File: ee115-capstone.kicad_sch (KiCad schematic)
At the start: 0 parts

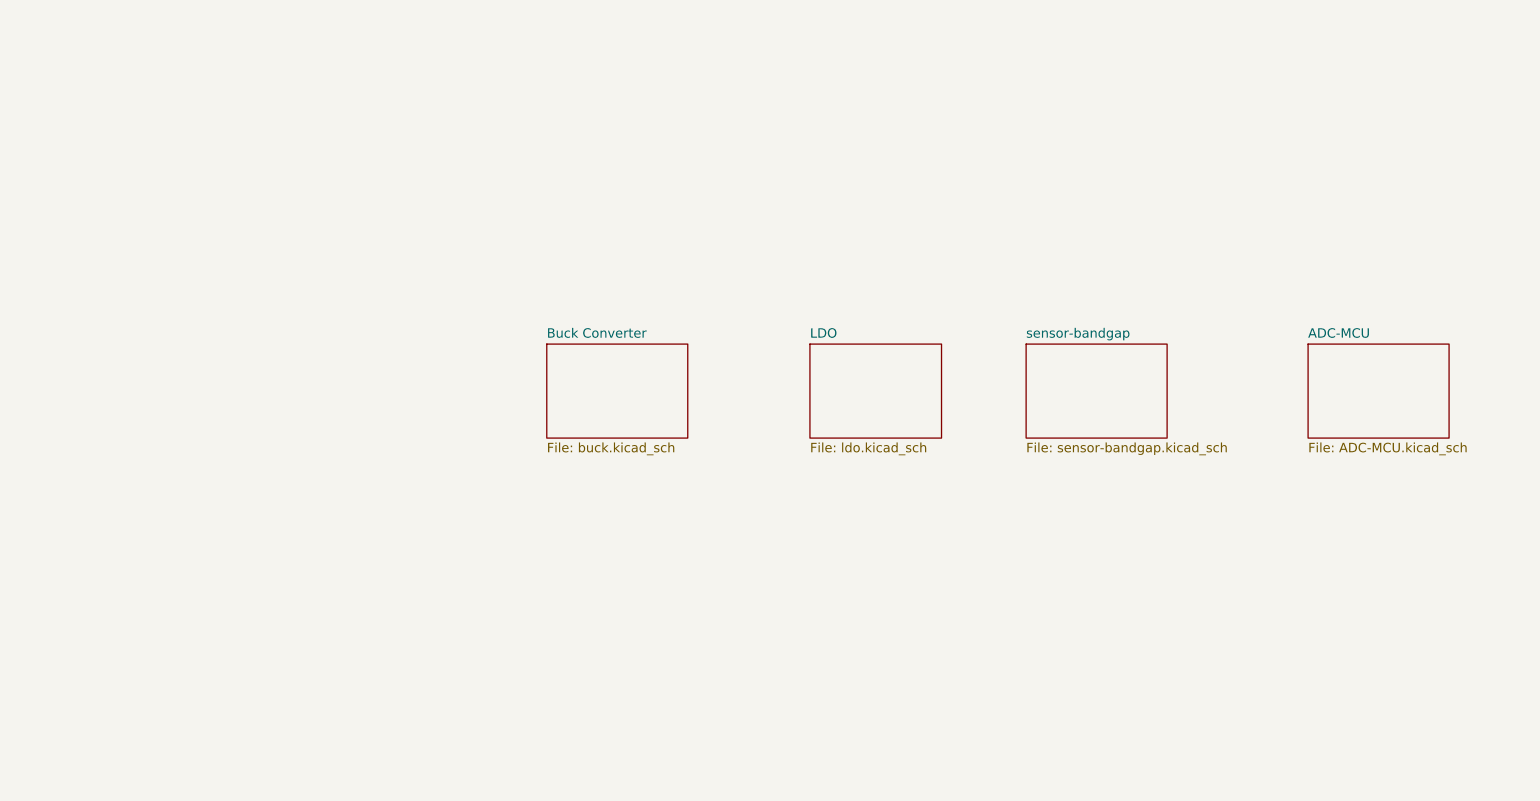
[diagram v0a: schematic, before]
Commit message: ADC-MCU and power latch
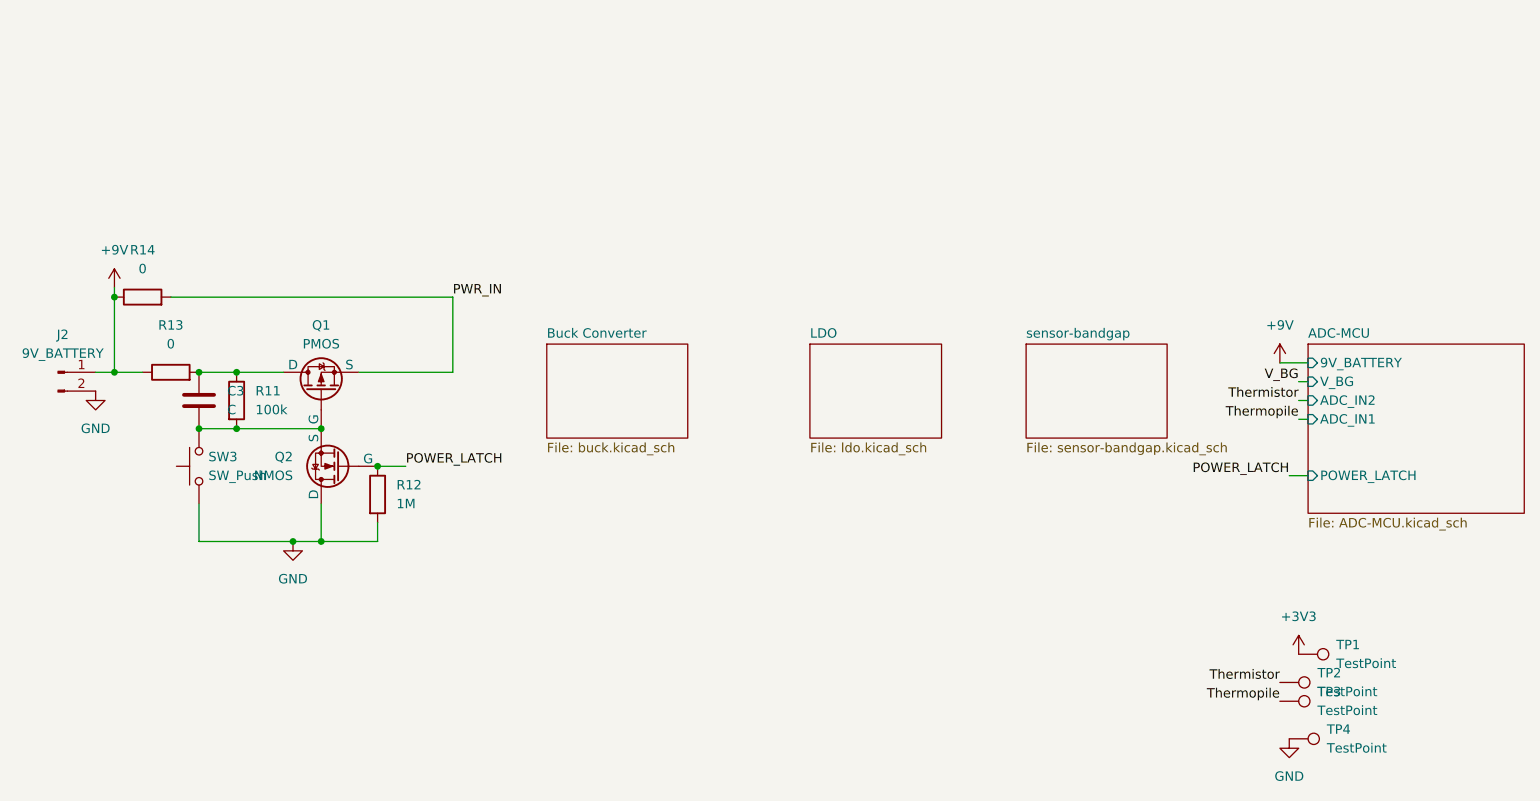
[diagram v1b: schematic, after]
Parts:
- added C3: C, Capacitor_SMD:C_0805_2012Metric, symbol Device:C
- added J2: 9V_BATTERY, Connector_JST:JST_PH_B2B-PH-K_1x02_P2.00mm_Vertical, symbol Connector:Conn_01x02_Pin
- added Q1: PMOS, symbol Simulation_SPICE:PMOS
- added Q2: NMOS, symbol Simulation_SPICE:NMOS
- added R11: 100k, Resistor_SMD:R_0805_2012Metric, symbol Device:R
- added R12: 1M, Resistor_SMD:R_0805_2012Metric, symbol Device:R
- added R13, R14: 0, Resistor_SMD:R_0805_2012Metric, symbol Device:R
- added SW3: SW_Push, Button_Switch_THT:SW_PUSH_6mm, symbol Switch:SW_Push
- added TP1, TP2, TP3, TP4: TestPoint, Connector_Pin:Pin_D1.0mm_L10.0mm, symbol Connector:TestPoint
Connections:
- new net: C3.1, Q1.1 (D), R11.1, R13.2
- new net: C3.2, Q1.2 (G), Q2.3 (S), R11.2, SW3.2
- new net +3V3: TP1.1
- new net +9V: J2.1 (Pin_1), R13.1, R14.1
- new net GND: J2.2 (Pin_2), Q2.1 (D), R12.2, SW3.1, TP4.1
- new net POWER_LATCH: Q2.2 (G), R12.1
- new net PWR_IN: Q1.3 (S), R14.2
- new net Thermistor: TP2.1
- new net Thermopile: TP3.1
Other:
- sheet ADC-MCU ports: added 9V_BATTERY, ADC_IN1, ADC_IN2, POWER_LATCH, V_BG; removed none

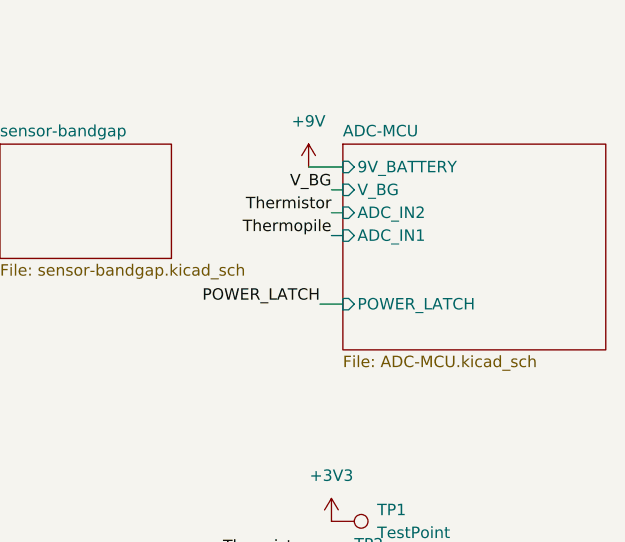
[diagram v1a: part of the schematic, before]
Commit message: added range sel
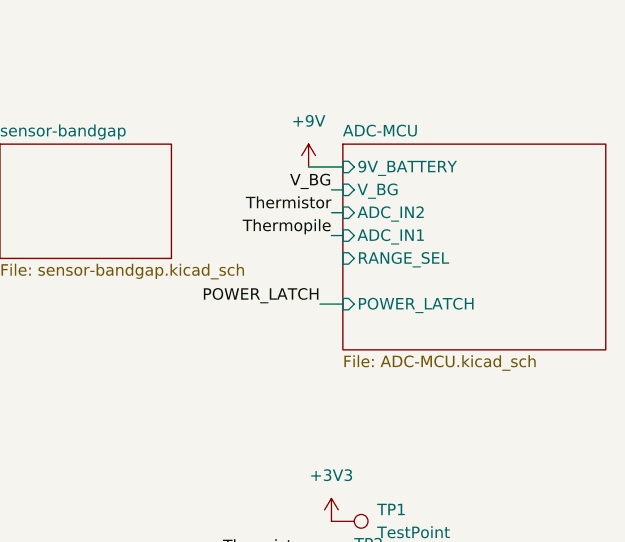
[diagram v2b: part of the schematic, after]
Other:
- sheet ADC-MCU ports: added RANGE_SEL; removed none
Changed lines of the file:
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@@
+			)
+		)
+		(pin "RANGE_SEL" input
+			(at 193.04 72.39 180)
+			(effects
+				(font
+					(size 1.27 1.27)
+				)
+				(justify left)
 			)
 		)

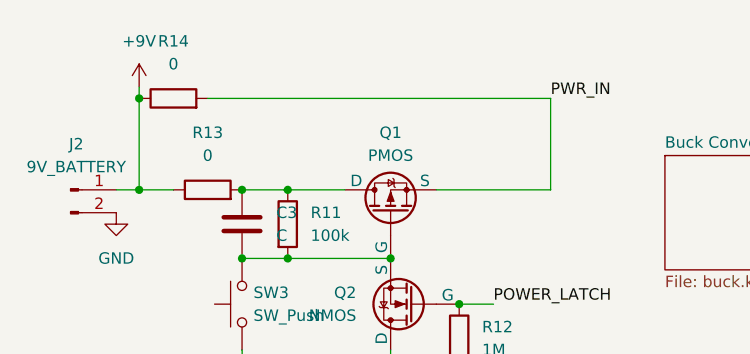
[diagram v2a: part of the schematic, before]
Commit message: added spst as backup to power latch
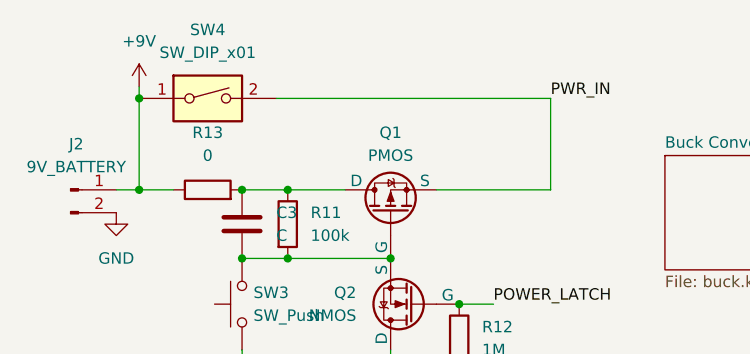
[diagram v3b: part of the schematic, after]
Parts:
- removed R14: 0, Resistor_SMD:R_0805_2012Metric, symbol Device:R
- added SW4: SW_DIP_x01, symbol Switch:SW_DIP_x01
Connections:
- net +9V: now also SW4.1
- net PWR_IN: now also SW4.2
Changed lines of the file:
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@@
+	)
+	(junction
+		(at 48.26 71.12)
+		(diameter 0)
+		(color 0 0 0 0)
+	)
+	(junction
+		(at 43.18 71.12)
+		(diameter 0)
+		(color 0 0 0 0)
+	)
+	(junction
+		(at 31.75 63.5)
+		(diameter 0)
+		(color 0 0 0 0)
 	)
 	(junction
@@
 		(color 0 0 0 0)
 	)
-	(junction
-		(at 48.26 71.12)
-		(diameter 0)
-		(color 0 0 0 0)
-	)
-	(junction
-		(at 43.18 71.12)
-		(diameter 0)
-		(color 0 0 0 0)
-	)
-	(junction
-		(at 31.75 63.5)
-		(diameter 0)
-		(color 0 0 0 0)
-	)
 	(wire
 		(pts
@@
 	(wire
 		(pts
+			(xy 46.99 53.34) (xy 77.47 53.34)
+		)
+		(stroke
+			(width 0)
+			(type default)
+		)
+	)
+	(wire
+		(pts
 			(xy 31.75 52.07) (xy 31.75 53.34)
 		)
@@
 	(wire
 		(pts
+			(xy 31.75 53.34) (xy 31.75 63.5)
+		)
+		(stroke
+			(width 0)
+			(type default)
+		)
+	)
+	(wire
+		(pts
 			(xy 71.12 76.2) (xy 67.31 76.2)
 		)
@@
 	(wire
 		(pts
-			(xy 31.75 53.34) (xy 31.75 63.5)
-		)
-		(stroke
-			(width 0)
-			(type default)
-		)
-	)
-	(wire
-		(pts
 			(xy 190.5 77.47) (xy 193.04 77.47)
 		)
@@
 		(pts
 			(xy 43.18 81.28) (xy 43.18 86.36)
-		)
-		(stroke
-			(width 0)
-			(type default)
-		)
-	)
-	(wire
-		(pts
-			(xy 39.37 53.34) (xy 77.47 53.34)
 		)
 		(stroke
@@
 	)
 	(symbol
-		(lib_id "Device:R")
-		(at 35.56 53.34 90)
-		(unit 1)
-		(exclude_from_sim no)
-		(in_bom yes)
-		(on_board yes)
-		(dnp no)
-		(fields_autoplaced yes)
-		(property "Reference" "R14"
-			(at 35.56 46.99 90)
-			(effects
-				(font
-					(size 1.27 1.27)
-				)
-			)
-		)
-		(property "Value" "0"
-			(at 35.56 49.53 90)
-			(effects
-				(font
-					(size 1.27 1.27)
-				)
-			)
-		)
-		(property "Footprint" "Resistor_SMD:R_0805_2012Metric"
-			(at 35.56 55.118 90)
-			(effects
-				(font
-					(size 1.27 1.27)
-				)
-				(hide yes)
-			)
-		)
-		(property "Datasheet" "~"
-			(at 35.56 53.34 0)
-			(effects
-				(font
-					(size 1.27 1.27)
-				)
-				(hide yes)
-			)
-		)
-		(property "Description" "Resistor"
-			(at 35.56 53.34 0)
-			(effects
-				(font
-					(size 1.27 1.27)
-				)
-				(hide yes)
-			)
-		)
-		(pin "1"
-		)
-		(pin "2"
-		)
-		(instances
-			(project "ee115-capstone"
-				(path "/80dfed98-7d85-4c9a-bb85-182165e7352f"
-					(reference "R14")
-					(unit 1)
-				)
-			)
-		)
-	)
-	(symbol
 		(lib_id "Switch:SW_Push")
 		(at 43.18 76.2 90)
@@
 					(unit 1)
 				)
+			)
+		)
+	)
+	(symbol
+		(lib_id "Switch:SW_DIP_x01")
+		(at 39.37 53.34 0)
+		(unit 1)
+		(exclude_from_sim no)
+		(in_bom yes)
+		(on_board yes)
+		(dnp no)
+		(fields_autoplaced yes)
+		(property "Reference" "SW4"
+			(at 39.37 45.72 0)
+			(effects
+				(font
+					(size 1.27 1.27)
+				)
+			)
+		)
+		(property "Value" "SW_DIP_x01"
+			(at 39.37 48.26 0)
+			(effects
+				(font
+					(size 1.27 1.27)
+				)
+			)
+		)
+		(property "Footprint" ""
+			(at 39.37 53.34 0)
+			(effects
+				(font
+					(size 1.27 1.27)
+				)
+				(hide yes)
+			)
+		)
+		(property "Datasheet" "~"
+			(at 39.37 53.34 0)
+			(effects
+				(font
+					(size 1.27 1.27)
+				)
+				(hide yes)
+			)
+		)
+		(property "Description" "1x DIP Switch, Single Pole Single Throw (SPST) switch, small symbol"
+			(at 39.37 53.34 0)
+			(effects
+				(font
+					(size 1.27 1.27)
+				)
+				(hide yes)
+			)
+		)
+		(pin "1"
+		)
+		(pin "2"
+		)
+		(instances
+			(project "ee115-capstone"
+				(path "/80dfed98-7d85-4c9a-bb85-182165e7352f"
+					(reference "SW4")
+					(unit 1)
+				)

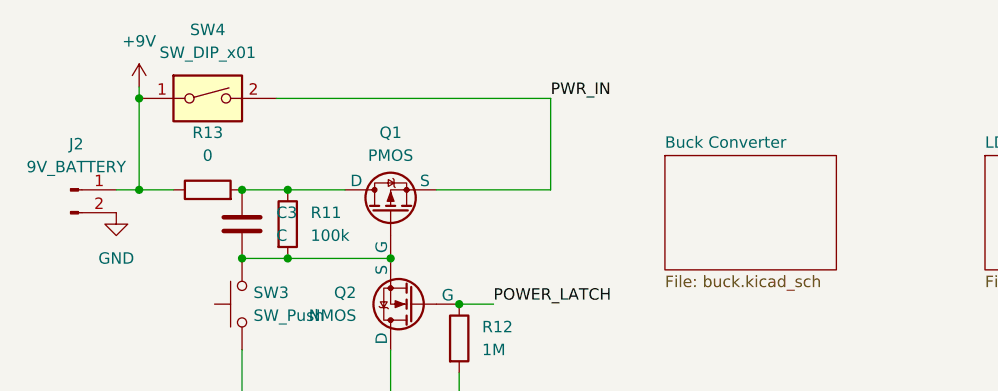
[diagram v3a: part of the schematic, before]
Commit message: added sawtooth gen
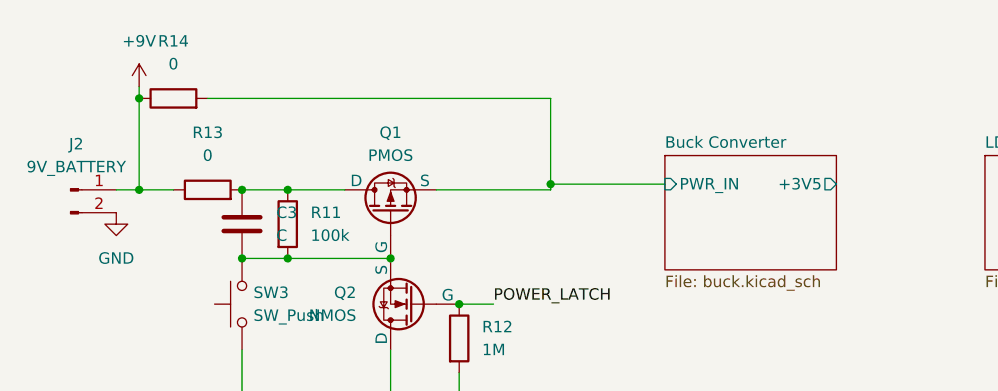
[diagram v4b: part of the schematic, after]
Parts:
- removed SW4: SW_DIP_x01, symbol Switch:SW_DIP_x01
- added R14: 0, Resistor_SMD:R_0805_2012Metric, symbol Device:R
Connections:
- net +9V: now also R14.1
- net PWR_IN renamed Buck Converter/PWR_IN
- net Buck Converter/PWR_IN: now also R14.2
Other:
- sheet Buck Converter ports: added +3V5, PWR_IN; removed none
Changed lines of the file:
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@@
+	)
+	(junction
+		(at 77.47 62.865)
+		(diameter 0)
+		(color 0 0 0 0)
 	)
 	(junction
@@
 	)
 	(junction
+		(at 31.75 53.34)
+		(diameter 0)
+		(color 0 0 0 0)
+	)
+	(junction
 		(at 48.26 71.12)
 		(diameter 0)
@@
 		(color 0 0 0 0)
 	)
-	(junction
-		(at 31.75 53.34)
-		(diameter 0)
-		(color 0 0 0 0)
-	)
 	(wire
 		(pts
@@
 	(wire
 		(pts
-			(xy 46.99 53.34) (xy 77.47 53.34)
+			(xy 77.47 62.865) (xy 77.47 63.5)
 		)
 		(stroke
@@
 	(wire
 		(pts
+			(xy 71.12 76.2) (xy 67.31 76.2)
+		)
+		(stroke
+			(width 0)
+			(type default)
+		)
+	)
+	(wire
+		(pts
+			(xy 48.26 71.12) (xy 59.69 71.12)
+		)
+		(stroke
+			(width 0)
+			(type default)
+		)
+	)
+	(wire
+		(pts
 			(xy 31.75 53.34) (xy 31.75 63.5)
 		)
@@
 	(wire
 		(pts
-			(xy 71.12 76.2) (xy 67.31 76.2)
-		)
-		(stroke
-			(width 0)
-			(type default)
-		)
-	)
-	(wire
-		(pts
-			(xy 48.26 71.12) (xy 59.69 71.12)
+			(xy 77.47 62.865) (xy 90.17 62.865)
 		)
 		(stroke
@@
 	(wire
 		(pts
+			(xy 39.37 53.34) (xy 77.47 53.34)
+		)
+		(stroke
+			(width 0)
+			(type default)
+		)
+	)
+	(wire
+		(pts
 			(xy 67.31 86.36) (xy 59.69 86.36)
 		)
@@
 	(wire
 		(pts
-			(xy 77.47 53.34) (xy 77.47 63.5)
+			(xy 77.47 53.34) (xy 77.47 62.865)
 		)
 		(stroke
@@
 		)
 	)
-	(label "PWR_IN"
-		(at 77.47 53.34 0)
-		(effects
-			(font
-				(size 1.27 1.27)
-			)
-			(justify left bottom)
-		)
-	)
 	(label "Thermopile"
 		(at 191.77 69.85 180)
@@
 	)
 	(symbol
+		(lib_id "Device:R")
+		(at 35.56 53.34 90)
+		(unit 1)
+		(exclude_from_sim no)
+		(in_bom yes)
+		(on_board yes)
+		(dnp no)
+		(fields_autoplaced yes)
+		(property "Reference" "R14"
+			(at 35.56 46.99 90)
+			(effects
+				(font
+					(size 1.27 1.27)
+				)
+			)
+		)
+		(property "Value" "0"
+			(at 35.56 49.53 90)
+			(effects
+				(font
+					(size 1.27 1.27)
+				)
+			)
+		)
+		(property "Footprint" "Resistor_SMD:R_0805_2012Metric"
+			(at 35.56 55.118 90)
+			(effects
+				(font
+					(size 1.27 1.27)
+				)
+				(hide yes)
+			)
+		)
+		(property "Datasheet" "~"
+			(at 35.56 53.34 0)
+			(effects
+				(font
+					(size 1.27 1.27)
+				)
+				(hide yes)
+			)
+		)
+		(property "Description" "Resistor"
+			(at 35.56 53.34 0)
+			(effects
+				(font
+					(size 1.27 1.27)
+				)
+				(hide yes)
+			)
+		)
+		(pin "1"
+		)
+		(pin "2"
+		)
+		(instances
+			(project "ee115-capstone"
+				(path "/80dfed98-7d85-4c9a-bb85-182165e7352f"
+					(reference "R14")
+					(unit 1)
+				)
+			)
+		)
+	)
+	(symbol
 		(lib_id "Switch:SW_Push")
 		(at 43.18 76.2 90)
@@
 				(path "/80dfed98-7d85-4c9a-bb85-182165e7352f"
 					(reference "SW3")
-					(unit 1)
-				)
-			)
-		)
-	)
-	(symbol
-		(lib_id "Switch:SW_DIP_x01")
-		(at 39.37 53.34 0)
-		(unit 1)
-		(exclude_from_sim no)
-		(in_bom yes)
-		(on_board yes)
-		(dnp no)
-		(fields_autoplaced yes)
-		(property "Reference" "SW4"
-			(at 39.37 45.72 0)
-			(effects
-				(font
-					(size 1.27 1.27)
-				)
-			)
-		)
-		(property "Value" "SW_DIP_x01"
-			(at 39.37 48.26 0)
-			(effects
-				(font
-					(size 1.27 1.27)
-				)
-			)
-		)
-		(property "Footprint" ""
-			(at 39.37 53.34 0)
-			(effects
-				(font
-					(size 1.27 1.27)
-				)
-				(hide yes)
-			)
-		)
-		(property "Datasheet" "~"
-			(at 39.37 53.34 0)
-			(effects
-				(font
-					(size 1.27 1.27)
-				)
-				(hide yes)
-			)
-		)
-		(property "Description" "1x DIP Switch, Single Pole Single Throw (SPST) switch, small symbol"
-			(at 39.37 53.34 0)
-			(effects
-				(font
-					(size 1.27 1.27)
-				)
-				(hide yes)
-			)
-		)
-		(pin "1"
-		)
-		(pin "2"
-		)
-		(instances
-			(project "ee115-capstone"
-				(path "/80dfed98-7d85-4c9a-bb85-182165e7352f"
-					(reference "SW4")
 					(unit 1)
 				)
@@
 			)
 		)
+		(pin "PWR_IN" input
+			(at 90.17 62.865 180)
+			(effects
+				(font
+					(size 1.27 1.27)
+				)
+				(justify left)
+			)
+		)
+		(pin "+3V5" output
+			(at 109.22 62.865 0)
+			(effects
+				(font
+					(size 1.27 1.27)
+				)
+				(justify right)
+			)
+		)
